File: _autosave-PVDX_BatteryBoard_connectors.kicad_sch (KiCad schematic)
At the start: 1 part, among them J1 Conn_01x06_Socket

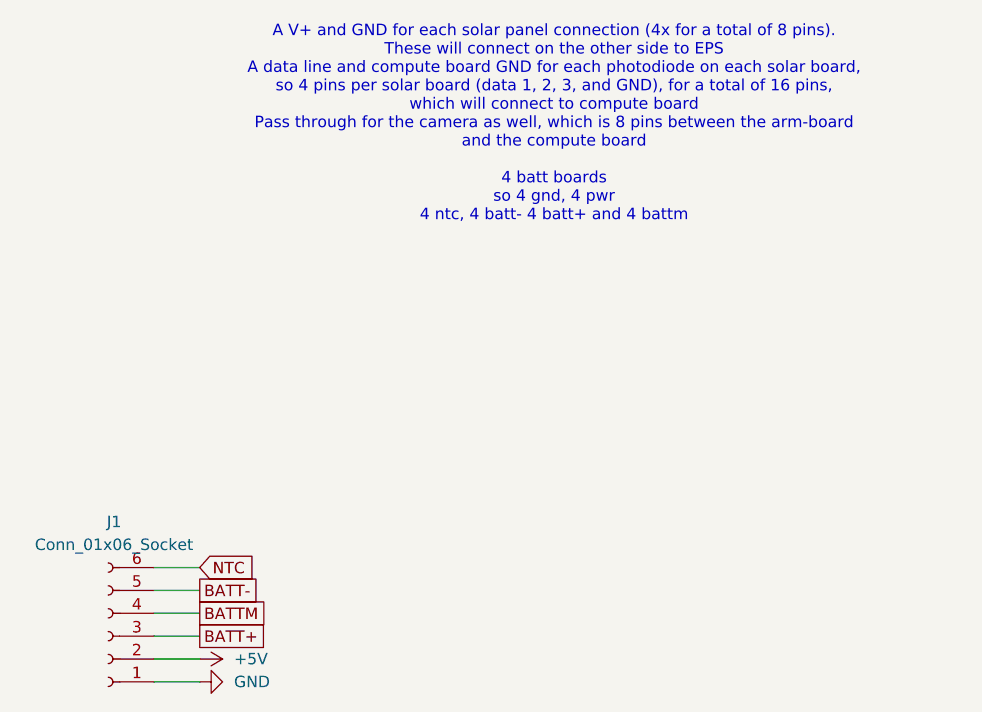
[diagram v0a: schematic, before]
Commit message: added solar connectors schematic
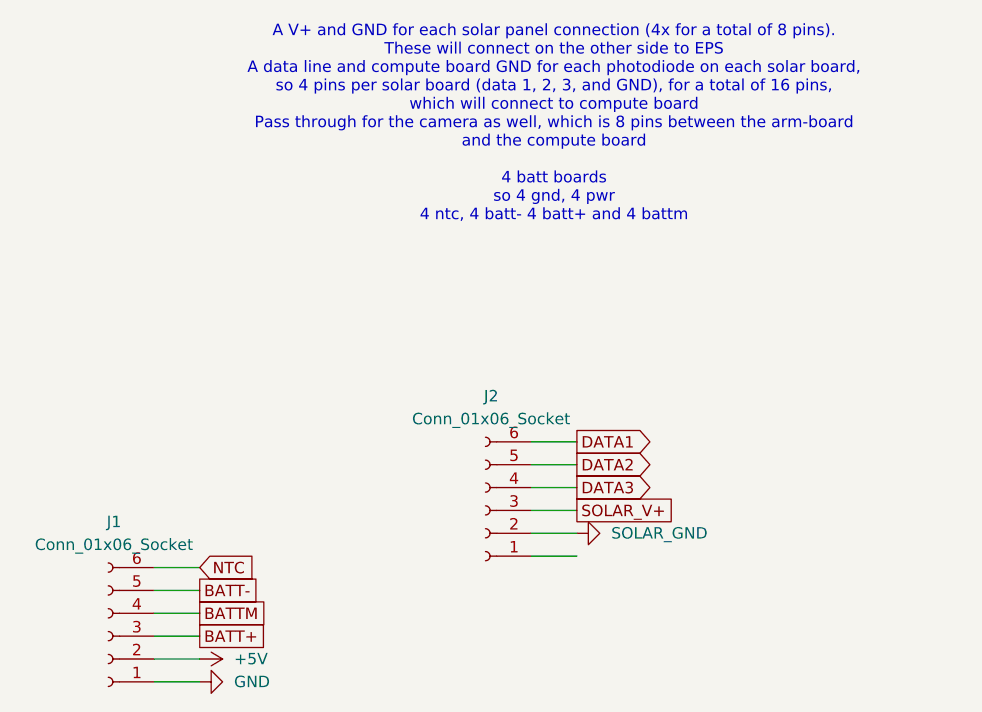
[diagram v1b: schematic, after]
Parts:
- added J2: Conn_01x06_Socket, symbol Connector:Conn_01x06_Socket
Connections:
- new net DATA1: J2.6 (Pin_6)
- new net DATA2: J2.5 (Pin_5)
- new net DATA3: J2.4 (Pin_4)
- new net SOLAR_GND: J2.2 (Pin_2)
- new net SOLAR_V+: J2.3 (Pin_3)
